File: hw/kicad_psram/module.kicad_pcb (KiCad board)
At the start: 8 copper layers, 110 x 70 mm, 20 parts

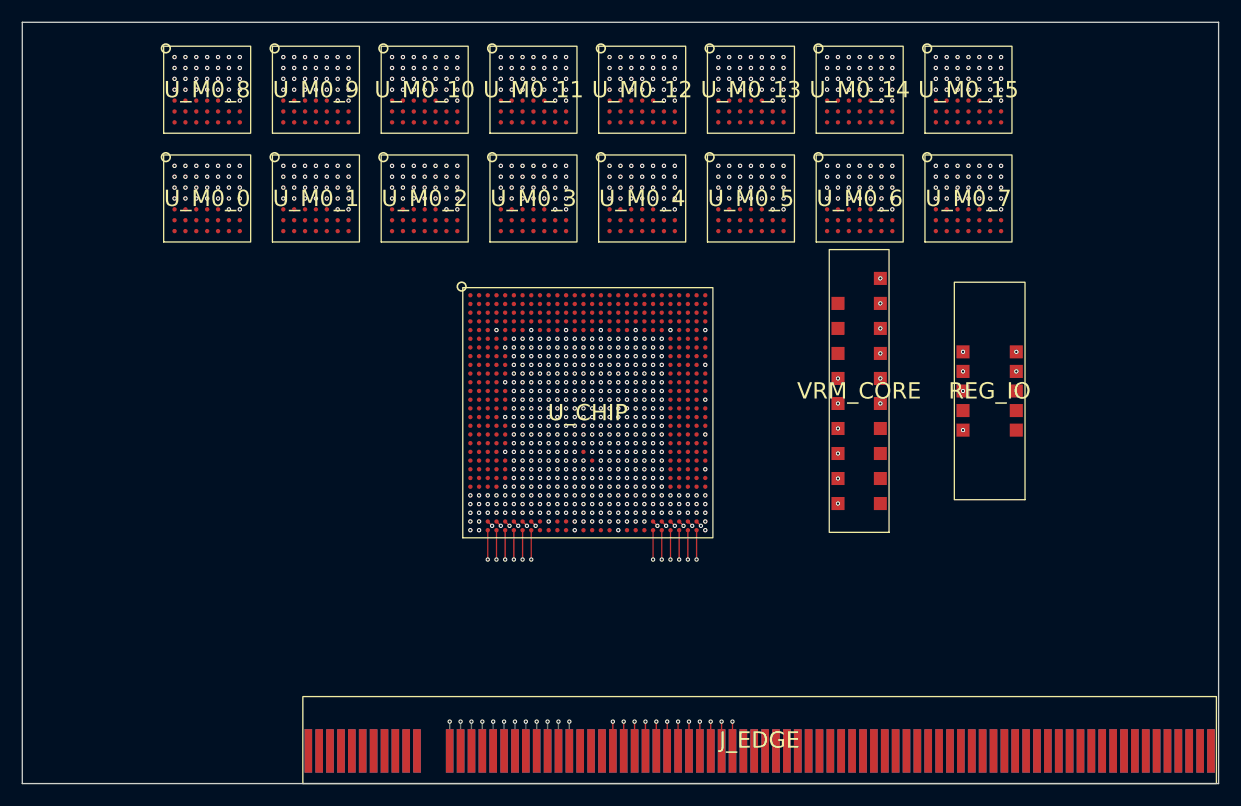
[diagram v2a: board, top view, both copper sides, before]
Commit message: Link in and out on the same finger positions: straight slot-to-slot hops
link_in sits on side A and link_out on side B of the same twelve edge
positions, so a slot's out-row pin faces the next slot's in-row pin and
every skip-one hop is a straight ribbon.  On the card the two drops from
the die's south-edge blocks lean towards one finger span from either side
and cross, so the out drop takes In3 and the two faces' vias interleave
half a position apart above the fingers.  The ribbon band narrows from
27 mm to 12, the stagger from 52 mm to 38, and the short board from 180 to
170 mm deep.  finger_layout: offset keeps the earlier separate spans.

Co-Authored-By: Claude Fable 5.1 <noreply@anthropic.com>
Claude-Session: https://claude.ai/code/session_01VmmvkZe8Ctg3RAykNGsQBn
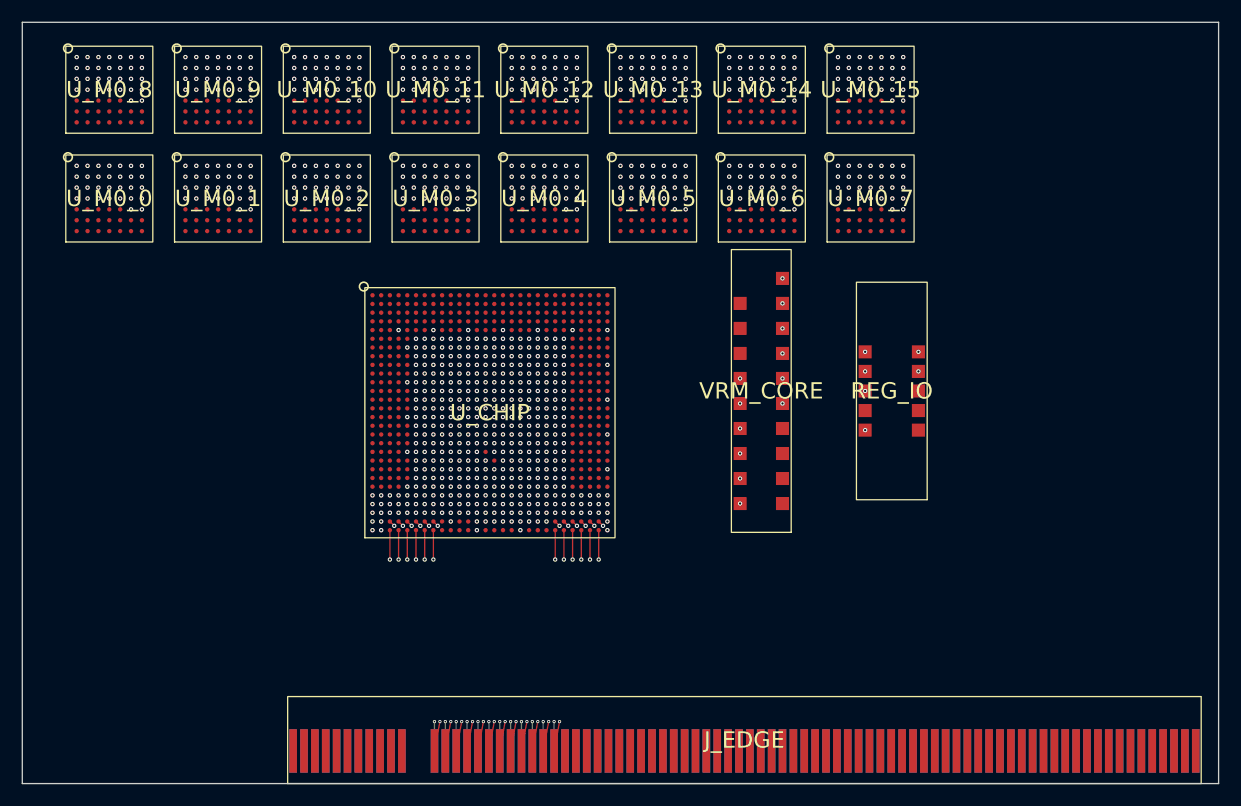
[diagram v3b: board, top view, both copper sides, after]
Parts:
- moved REG_IO 9.00 mm to (100.0, 53.9)
- moved U_CHIP 9.00 mm to (63.0, 55.9)
- moved U_M0_0 9.00 mm to (28.0, 36.2)
- moved U_M0_1 9.00 mm to (38.0, 36.2)
- moved U_M0_10 9.00 mm to (48.0, 26.2)
- moved U_M0_11 9.00 mm to (58.0, 26.2)
- moved U_M0_12 9.00 mm to (68.0, 26.2)
- moved U_M0_13 9.00 mm to (78.0, 26.2)
- moved U_M0_14 9.00 mm to (88.0, 26.2)
- moved U_M0_15 9.00 mm to (98.0, 26.2)
- moved U_M0_2 9.00 mm to (48.0, 36.2)
- moved U_M0_3 9.00 mm to (58.0, 36.2)
- moved U_M0_4 9.00 mm to (68.0, 36.2)
- moved U_M0_5 9.00 mm to (78.0, 36.2)
- moved U_M0_6 9.00 mm to (88.0, 36.2)
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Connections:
- J_EDGE pad B12: GND -> LINK_OUT_DATA0
- J_EDGE pad B13: GND -> LINK_OUT_DATA1
- J_EDGE pad B14: GND -> LINK_OUT_DATA2
- J_EDGE pad B15: GND -> LINK_OUT_DATA3
- J_EDGE pad B16: GND -> LINK_OUT_DATA4
- J_EDGE pad B17: GND -> LINK_OUT_DATA5
- J_EDGE pad B18: GND -> LINK_OUT_DATA6
- J_EDGE pad B19: GND -> LINK_OUT_DATA7
- J_EDGE pad B20: GND -> LINK_OUT_CLOCK
- J_EDGE pad B21: GND -> LINK_OUT_VALID
- J_EDGE pad B22: GND -> LINK_OUT_READY_BACK
- J_EDGE pad B23: GND -> LINK_OUT_SOF
- J_EDGE pad B27: LINK_OUT_DATA0 -> GND
- J_EDGE pad B28: LINK_OUT_DATA1 -> GND
- J_EDGE pad B29: LINK_OUT_DATA2 -> GND
- J_EDGE pad B30: LINK_OUT_DATA3 -> GND
- J_EDGE pad B31: LINK_OUT_DATA4 -> GND
- J_EDGE pad B32: LINK_OUT_DATA5 -> GND
- J_EDGE pad B33: LINK_OUT_DATA6 -> GND
- J_EDGE pad B34: LINK_OUT_DATA7 -> GND
- J_EDGE pad B35: LINK_OUT_CLOCK -> GND
- J_EDGE pad B36: LINK_OUT_VALID -> GND
- J_EDGE pad B37: LINK_OUT_READY_BACK -> GND
- J_EDGE pad B38: LINK_OUT_SOF -> GND
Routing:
- net LINK_IN_DATA0: track 21.3 -> 25.1 mm
- net LINK_OUT_SOF: track 22.3 -> 26.0 mm
- net LINK_IN_DATA1: track 21.9 -> 25.4 mm
- net LINK_OUT_READY_BACK: track 21.0 -> 24.4 mm
- net LINK_IN_DATA2: track 20.7 -> 23.9 mm
- net LINK_OUT_VALID: track 21.7 -> 24.8 mm
- net LINK_OUT_DATA0: track 21.3 -> 24.3 mm
- net LINK_IN_SOF: track 22.3 -> 25.3 mm
- net LINK_IN_READY_BACK: track 21.0 -> 23.9 mm
- net LINK_OUT_DATA1: track 22.0 -> 24.9 mm
- net LINK_IN_DATA3: track 21.5 -> 24.3 mm
- net LINK_IN_VALID: track 21.7 -> 24.5 mm
- net LINK_OUT_DATA2: track 20.7 -> 23.6 mm
- net LINK_OUT_CLOCK: track 20.5 -> 23.4 mm
- net LINK_IN_CLOCK: track 20.5 -> 23.2 mm
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
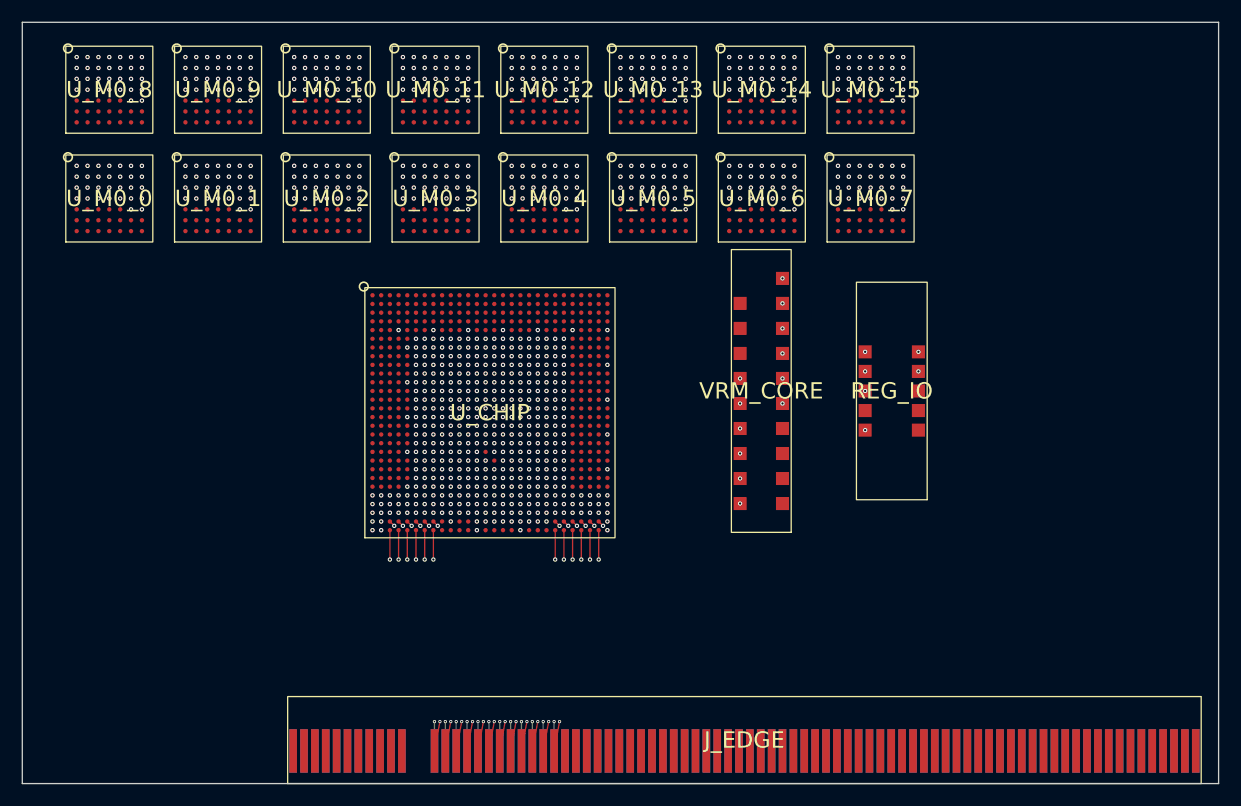
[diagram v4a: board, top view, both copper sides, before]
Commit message: Choose the PSRAM and write its HPI controller
The PSRAM board's device is the AP Memory APS512XXN-OB9-BG: 512 Mb, the
Xccela DDR interface in x16 (HPI) mode, 250 MHz, 1.8 V, a 24-ball 6 x 8
mm BGA.  fabric/hpi.py carries its geometry, the mode-register
encodings, the command frame and the striping of the die's memory port
over sixteen devices in page-sized stripes; fabric_hpi.sv is the
controller: a per-device channel with the power-up sequence, global
reset, mode registers and an identity check, the command phase on both
clock edges, fixed-latency writes with data mask, and reads captured by
the device's strobe through a gray-pointer ring so refresh push-out
costs nothing; and a stripe unit that splits a burst into concurrent
per-device chunks, returns read data in order and completes a write
only when every chunk is in the device.  A behavioural device model
checks the protocol (tCEM, tCPH, even addresses, x16 mode) and the
testbench runs random bursts over one, two, four and sixteen devices
against the striped image.

The memory port's burst count widens to 12 bits so a head's state is
one burst across all devices, and the map aligns regions to a page.
The board gains the real part, its DQS/DM naming, and the four shared
clocks as a small interface the pinout places with the management
signals and the card wires to its devices; the connector count is
unchanged.

Co-Authored-By: Claude Fable 5.1 <noreply@anthropic.com>
Claude-Session: https://claude.ai/code/session_01VmmvkZe8Ctg3RAykNGsQBn
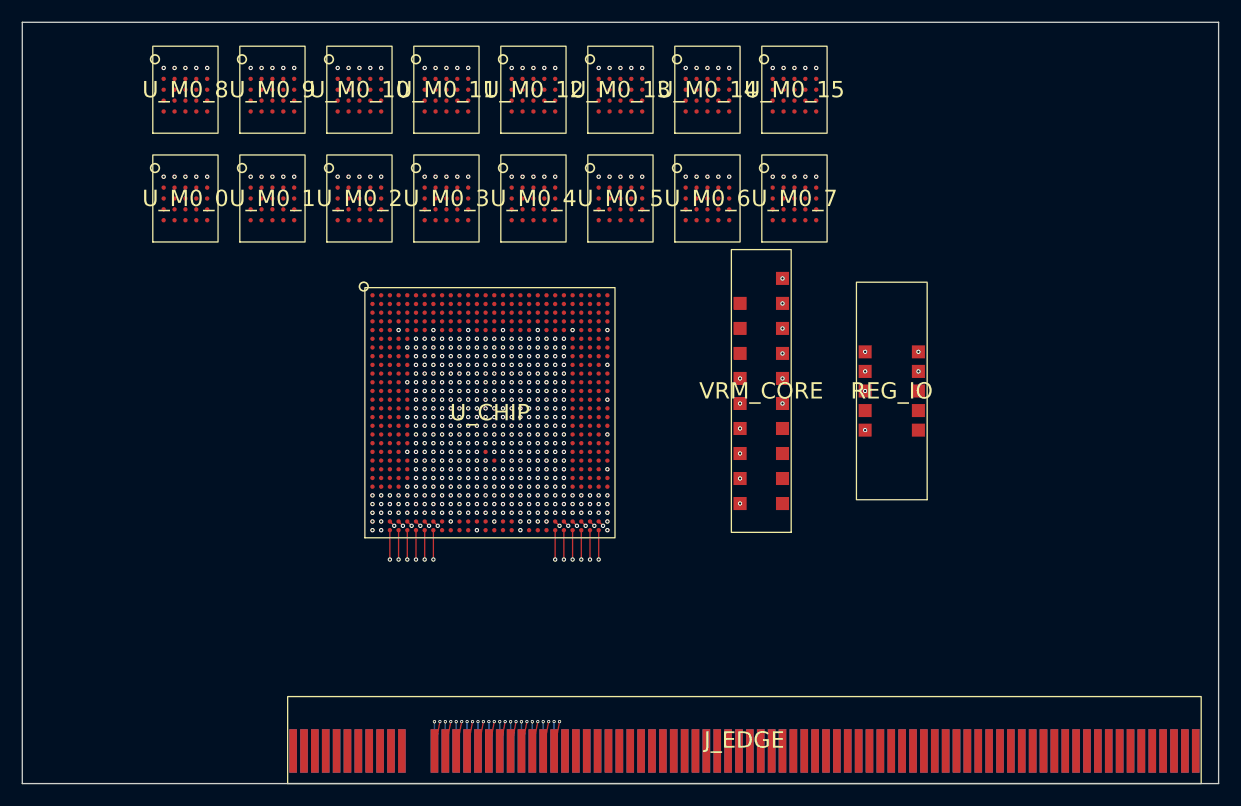
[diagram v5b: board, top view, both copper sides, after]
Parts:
- U_M0_0, U_M0_1, U_M0_10, U_M0_11, U_M0_12, U_M0_13, U_M0_14, U_M0_15, U_M0_2, U_M0_3, U_M0_4, U_M0_5, U_M0_6, U_M0_7, U_M0_8, U_M0_9: footprint appliance:FBGA49_7x7_P1.0 -> appliance:BGA24_5x5_P1.0
- moved U_M0_0 7.00 mm to (35.0, 36.2)
- moved U_M0_15 7.00 mm to (91.0, 26.2)
- moved U_M0_7 7.00 mm to (91.0, 36.2)
- moved U_M0_8 7.00 mm to (35.0, 26.2)
- moved U_M0_1 5.00 mm to (43.0, 36.2)
- moved U_M0_14 5.00 mm to (83.0, 26.2)
- moved U_M0_6 5.00 mm to (83.0, 36.2)
- moved U_M0_9 5.00 mm to (43.0, 26.2)
- moved U_M0_10 3.00 mm to (51.0, 26.2)
- moved U_M0_13 3.00 mm to (75.0, 26.2)
- moved U_M0_2 3.00 mm to (51.0, 36.2)
- moved U_M0_5 3.00 mm to (75.0, 36.2)
- moved U_M0_11 1.00 mm to (59.0, 26.2)
- moved U_M0_12 1.00 mm to (67.0, 26.2)
- moved U_M0_3 1.00 mm to (59.0, 36.2)
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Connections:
- net PSRAM_0_CS renamed PSRAM_0_CE
- net PSRAM_0_RWDS0 renamed PSRAM_0_DQS0
- net PSRAM_0_RWDS1 renamed PSRAM_0_DQS1
- net PSRAM_10_CS renamed PSRAM_10_CE
- net PSRAM_10_RWDS0 renamed PSRAM_10_DQS0
- net PSRAM_10_RWDS1 renamed PSRAM_10_DQS1
- net PSRAM_11_CS renamed PSRAM_11_CE
- net PSRAM_11_RWDS0 renamed PSRAM_11_DQS0
- net PSRAM_11_RWDS1 renamed PSRAM_11_DQS1
- net PSRAM_12_CS renamed PSRAM_12_CE
- net PSRAM_12_RWDS0 renamed PSRAM_12_DQS0
- net PSRAM_12_RWDS1 renamed PSRAM_12_DQS1
- net PSRAM_13_CS renamed PSRAM_13_CE
- net PSRAM_13_RWDS0 renamed PSRAM_13_DQS0
- net PSRAM_13_RWDS1 renamed PSRAM_13_DQS1
- net PSRAM_14_CS renamed PSRAM_14_CE
- net PSRAM_14_RWDS0 renamed PSRAM_14_DQS0
- net PSRAM_14_RWDS1 renamed PSRAM_14_DQS1
- net PSRAM_15_CS renamed PSRAM_15_CE
- net PSRAM_15_RWDS0 renamed PSRAM_15_DQS0
- net PSRAM_15_RWDS1 renamed PSRAM_15_DQS1
- net PSRAM_1_CS renamed PSRAM_1_CE
- net PSRAM_1_RWDS0 renamed PSRAM_1_DQS0
- net PSRAM_1_RWDS1 renamed PSRAM_1_DQS1
- net PSRAM_2_CS renamed PSRAM_2_CE
- net PSRAM_2_RWDS0 renamed PSRAM_2_DQS0
- net PSRAM_2_RWDS1 renamed PSRAM_2_DQS1
- net PSRAM_3_CS renamed PSRAM_3_CE
- net PSRAM_3_RWDS0 renamed PSRAM_3_DQS0
- net PSRAM_3_RWDS1 renamed PSRAM_3_DQS1
- net PSRAM_4_CS renamed PSRAM_4_CE
- net PSRAM_4_RWDS0 renamed PSRAM_4_DQS0
- net PSRAM_4_RWDS1 renamed PSRAM_4_DQS1
- net PSRAM_5_CS renamed PSRAM_5_CE
- net PSRAM_5_RWDS0 renamed PSRAM_5_DQS0
- net PSRAM_5_RWDS1 renamed PSRAM_5_DQS1
- net PSRAM_6_CS renamed PSRAM_6_CE
- net PSRAM_6_RWDS0 renamed PSRAM_6_DQS0
- net PSRAM_6_RWDS1 renamed PSRAM_6_DQS1
- net PSRAM_7_CS renamed PSRAM_7_CE
- net PSRAM_7_RWDS0 renamed PSRAM_7_DQS0
- net PSRAM_7_RWDS1 renamed PSRAM_7_DQS1
- net PSRAM_8_CS renamed PSRAM_8_CE
- net PSRAM_8_RWDS0 renamed PSRAM_8_DQS0
- net PSRAM_8_RWDS1 renamed PSRAM_8_DQS1
- net PSRAM_9_CS renamed PSRAM_9_CE
- net PSRAM_9_RWDS0 renamed PSRAM_9_DQS0
- net PSRAM_9_RWDS1 renamed PSRAM_9_DQS1
- U_CHIP pad AG13: GND -> PSRAM_CLK0
- U_CHIP pad AG14: VDD_CORE -> PSRAM_CLK1
- U_CHIP pad AG16: VDD_CORE -> PSRAM_CLK2
- U_CHIP pad AG17: GND -> PSRAM_CLK3
- U_M0_0 pad B1: VDD_IO_1V8 -> MEM0_DQ15
- U_M0_0 pad B2: GND -> MEM0_DQS0
- U_M0_0 pad B3: VDD_IO_1V8 -> MEM0_DQS1
- U_M0_0 pad B4: GND -> MEM0_CE
- U_M0_0 pad B5: VDD_IO_1V8 -> PSRAM_CLK0
- U_M0_0 pad C1: GND -> MEM0_DQ10
- U_M0_0 pad C2: VDD_IO_1V8 -> MEM0_DQ11
- U_M0_0 pad C3: GND -> MEM0_DQ12
- U_M0_0 pad C4: VDD_IO_1V8 -> MEM0_DQ13
- U_M0_0 pad C5: GND -> MEM0_DQ14
- U_M0_0 pad D1: VDD_IO_1V8 -> MEM0_DQ5
- U_M0_0 pad D2: GND -> MEM0_DQ6
- U_M0_0 pad D3: VDD_IO_1V8 -> MEM0_DQ7
- U_M0_0 pad D4: GND -> MEM0_DQ8
- U_M0_0 pad D5: VDD_IO_1V8 -> MEM0_DQ9
- U_M0_0 pad E1: MEM0_DQ14 -> MEM0_DQ0
- U_M0_0 pad E2: MEM0_DQ15 -> MEM0_DQ1
- U_M0_0 pad E3: MEM0_RWDS0 -> MEM0_DQ2
- U_M0_0 pad E4: MEM0_RWDS1 -> MEM0_DQ3
- U_M0_0 pad E5: MEM0_CS -> MEM0_DQ4
- U_M0_1 pad B1: VDD_IO_1V8 -> MEM1_DQ15
- U_M0_1 pad B2: GND -> MEM1_DQS0
- U_M0_1 pad B3: VDD_IO_1V8 -> MEM1_DQS1
- U_M0_1 pad B4: GND -> MEM1_CE
- U_M0_1 pad B5: VDD_IO_1V8 -> PSRAM_CLK0
- U_M0_1 pad C1: GND -> MEM1_DQ10
- U_M0_1 pad C2: VDD_IO_1V8 -> MEM1_DQ11
- U_M0_1 pad C3: GND -> MEM1_DQ12
- U_M0_1 pad C4: VDD_IO_1V8 -> MEM1_DQ13
- U_M0_1 pad C5: GND -> MEM1_DQ14
- U_M0_1 pad D1: VDD_IO_1V8 -> MEM1_DQ5
- U_M0_1 pad D2: GND -> MEM1_DQ6
- U_M0_1 pad D3: VDD_IO_1V8 -> MEM1_DQ7
- U_M0_1 pad D4: GND -> MEM1_DQ8
- U_M0_1 pad D5: VDD_IO_1V8 -> MEM1_DQ9
- U_M0_1 pad E1: MEM1_DQ14 -> MEM1_DQ0
- U_M0_1 pad E2: MEM1_DQ15 -> MEM1_DQ1
- U_M0_1 pad E3: MEM1_RWDS0 -> MEM1_DQ2
- U_M0_1 pad E4: MEM1_RWDS1 -> MEM1_DQ3
- U_M0_1 pad E5: MEM1_CS -> MEM1_DQ4
- U_M0_10 pad B1: VDD_IO_1V8 -> MEM10_DQ15
- U_M0_10 pad B2: GND -> MEM10_DQS0
- U_M0_10 pad B3: VDD_IO_1V8 -> MEM10_DQS1
- U_M0_10 pad B4: GND -> MEM10_CE
- U_M0_10 pad B5: VDD_IO_1V8 -> PSRAM_CLK2
- U_M0_10 pad C1: GND -> MEM10_DQ10
- U_M0_10 pad C2: VDD_IO_1V8 -> MEM10_DQ11
- U_M0_10 pad C3: GND -> MEM10_DQ12
- U_M0_10 pad C4: VDD_IO_1V8 -> MEM10_DQ13
- U_M0_10 pad C5: GND -> MEM10_DQ14
- U_M0_10 pad D1: VDD_IO_1V8 -> MEM10_DQ5
- U_M0_10 pad D2: GND -> MEM10_DQ6
- U_M0_10 pad D3: VDD_IO_1V8 -> MEM10_DQ7
- U_M0_10 pad D4: GND -> MEM10_DQ8
- U_M0_10 pad D5: VDD_IO_1V8 -> MEM10_DQ9
- U_M0_10 pad E1: MEM10_DQ14 -> MEM10_DQ0
- U_M0_10 pad E2: MEM10_DQ15 -> MEM10_DQ1
- U_M0_10 pad E3: MEM10_RWDS0 -> MEM10_DQ2
- U_M0_10 pad E4: MEM10_RWDS1 -> MEM10_DQ3
- U_M0_10 pad E5: MEM10_CS -> MEM10_DQ4
- U_M0_11 pad B1: VDD_IO_1V8 -> MEM11_DQ15
- U_M0_11 pad B2: GND -> MEM11_DQS0
- U_M0_11 pad B3: VDD_IO_1V8 -> MEM11_DQS1
- U_M0_11 pad B4: GND -> MEM11_CE
- U_M0_11 pad B5: VDD_IO_1V8 -> PSRAM_CLK2
- U_M0_11 pad C1: GND -> MEM11_DQ10
- U_M0_11 pad C2: VDD_IO_1V8 -> MEM11_DQ11
- U_M0_11 pad C3: GND -> MEM11_DQ12
- U_M0_11 pad C4: VDD_IO_1V8 -> MEM11_DQ13
- U_M0_11 pad C5: GND -> MEM11_DQ14
- U_M0_11 pad D1: VDD_IO_1V8 -> MEM11_DQ5
- U_M0_11 pad D2: GND -> MEM11_DQ6
- U_M0_11 pad D3: VDD_IO_1V8 -> MEM11_DQ7
- U_M0_11 pad D4: GND -> MEM11_DQ8
- U_M0_11 pad D5: VDD_IO_1V8 -> MEM11_DQ9
- U_M0_11 pad E1: MEM11_DQ14 -> MEM11_DQ0
- U_M0_11 pad E2: MEM11_DQ15 -> MEM11_DQ1
- U_M0_11 pad E3: MEM11_RWDS0 -> MEM11_DQ2
- U_M0_11 pad E4: MEM11_RWDS1 -> MEM11_DQ3
- U_M0_11 pad E5: MEM11_CS -> MEM11_DQ4
- U_M0_12 pad B1: VDD_IO_1V8 -> MEM12_DQ15
- U_M0_12 pad B2: GND -> MEM12_DQS0
- U_M0_12 pad B3: VDD_IO_1V8 -> MEM12_DQS1
- U_M0_12 pad B4: GND -> MEM12_CE
- U_M0_12 pad B5: VDD_IO_1V8 -> PSRAM_CLK3
- U_M0_12 pad C1: GND -> MEM12_DQ10
- U_M0_12 pad C2: VDD_IO_1V8 -> MEM12_DQ11
- U_M0_12 pad C3: GND -> MEM12_DQ12
- U_M0_12 pad C4: VDD_IO_1V8 -> MEM12_DQ13
- U_M0_12 pad C5: GND -> MEM12_DQ14
- U_M0_12 pad D1: VDD_IO_1V8 -> MEM12_DQ5
- U_M0_12 pad D2: GND -> MEM12_DQ6
- U_M0_12 pad D3: VDD_IO_1V8 -> MEM12_DQ7
- U_M0_12 pad D4: GND -> MEM12_DQ8
- U_M0_12 pad D5: VDD_IO_1V8 -> MEM12_DQ9
- U_M0_12 pad E1: MEM12_DQ14 -> MEM12_DQ0
- U_M0_12 pad E2: MEM12_DQ15 -> MEM12_DQ1
- U_M0_12 pad E3: MEM12_RWDS0 -> MEM12_DQ2
- U_M0_12 pad E4: MEM12_RWDS1 -> MEM12_DQ3
- U_M0_12 pad E5: MEM12_CS -> MEM12_DQ4
- U_M0_13 pad B1: VDD_IO_1V8 -> MEM13_DQ15
- U_M0_13 pad B2: GND -> MEM13_DQS0
- U_M0_13 pad B3: VDD_IO_1V8 -> MEM13_DQS1
- U_M0_13 pad B4: GND -> MEM13_CE
- U_M0_13 pad B5: VDD_IO_1V8 -> PSRAM_CLK3
- U_M0_13 pad C1: GND -> MEM13_DQ10
- U_M0_13 pad C2: VDD_IO_1V8 -> MEM13_DQ11
- U_M0_13 pad C3: GND -> MEM13_DQ12
- U_M0_13 pad C4: VDD_IO_1V8 -> MEM13_DQ13
- U_M0_13 pad C5: GND -> MEM13_DQ14
- U_M0_13 pad D1: VDD_IO_1V8 -> MEM13_DQ5
- U_M0_13 pad D2: GND -> MEM13_DQ6
- U_M0_13 pad D3: VDD_IO_1V8 -> MEM13_DQ7
- U_M0_13 pad D4: GND -> MEM13_DQ8
- U_M0_13 pad D5: VDD_IO_1V8 -> MEM13_DQ9
- U_M0_13 pad E1: MEM13_DQ14 -> MEM13_DQ0
- U_M0_13 pad E2: MEM13_DQ15 -> MEM13_DQ1
- U_M0_13 pad E3: MEM13_RWDS0 -> MEM13_DQ2
- U_M0_13 pad E4: MEM13_RWDS1 -> MEM13_DQ3
- U_M0_13 pad E5: MEM13_CS -> MEM13_DQ4
- U_M0_14 pad B1: VDD_IO_1V8 -> MEM14_DQ15
- U_M0_14 pad B2: GND -> MEM14_DQS0
- U_M0_14 pad B3: VDD_IO_1V8 -> MEM14_DQS1
- U_M0_14 pad B4: GND -> MEM14_CE
- U_M0_14 pad B5: VDD_IO_1V8 -> PSRAM_CLK3
- U_M0_14 pad C1: GND -> MEM14_DQ10
- U_M0_14 pad C2: VDD_IO_1V8 -> MEM14_DQ11
- U_M0_14 pad C3: GND -> MEM14_DQ12
- U_M0_14 pad C4: VDD_IO_1V8 -> MEM14_DQ13
- U_M0_14 pad C5: GND -> MEM14_DQ14
- U_M0_14 pad D1: VDD_IO_1V8 -> MEM14_DQ5
- U_M0_14 pad D2: GND -> MEM14_DQ6
- U_M0_14 pad D3: VDD_IO_1V8 -> MEM14_DQ7
- U_M0_14 pad D4: GND -> MEM14_DQ8
- U_M0_14 pad D5: VDD_IO_1V8 -> MEM14_DQ9
- U_M0_14 pad E1: MEM14_DQ14 -> MEM14_DQ0
- U_M0_14 pad E2: MEM14_DQ15 -> MEM14_DQ1
- U_M0_14 pad E3: MEM14_RWDS0 -> MEM14_DQ2
- U_M0_14 pad E4: MEM14_RWDS1 -> MEM14_DQ3
- U_M0_14 pad E5: MEM14_CS -> MEM14_DQ4
- U_M0_15 pad B1: VDD_IO_1V8 -> MEM15_DQ15
- U_M0_15 pad B2: GND -> MEM15_DQS0
- U_M0_15 pad B3: VDD_IO_1V8 -> MEM15_DQS1
- U_M0_15 pad B4: GND -> MEM15_CE
- U_M0_15 pad B5: VDD_IO_1V8 -> PSRAM_CLK3
- U_M0_15 pad C1: GND -> MEM15_DQ10
- U_M0_15 pad C2: VDD_IO_1V8 -> MEM15_DQ11
- U_M0_15 pad C3: GND -> MEM15_DQ12
- U_M0_15 pad C4: VDD_IO_1V8 -> MEM15_DQ13
- U_M0_15 pad C5: GND -> MEM15_DQ14
- U_M0_15 pad D1: VDD_IO_1V8 -> MEM15_DQ5
- U_M0_15 pad D2: GND -> MEM15_DQ6
- U_M0_15 pad D3: VDD_IO_1V8 -> MEM15_DQ7
- U_M0_15 pad D4: GND -> MEM15_DQ8
- U_M0_15 pad D5: VDD_IO_1V8 -> MEM15_DQ9
- U_M0_15 pad E1: MEM15_DQ14 -> MEM15_DQ0
- U_M0_15 pad E2: MEM15_DQ15 -> MEM15_DQ1
- U_M0_15 pad E3: MEM15_RWDS0 -> MEM15_DQ2
- U_M0_15 pad E4: MEM15_RWDS1 -> MEM15_DQ3
- U_M0_15 pad E5: MEM15_CS -> MEM15_DQ4
- U_M0_2 pad B1: VDD_IO_1V8 -> MEM2_DQ15
- U_M0_2 pad B2: GND -> MEM2_DQS0
- U_M0_2 pad B3: VDD_IO_1V8 -> MEM2_DQS1
- U_M0_2 pad B4: GND -> MEM2_CE
- U_M0_2 pad B5: VDD_IO_1V8 -> PSRAM_CLK0
- U_M0_2 pad C1: GND -> MEM2_DQ10
- U_M0_2 pad C2: VDD_IO_1V8 -> MEM2_DQ11
- U_M0_2 pad C3: GND -> MEM2_DQ12
- U_M0_2 pad C4: VDD_IO_1V8 -> MEM2_DQ13
- U_M0_2 pad C5: GND -> MEM2_DQ14
- U_M0_2 pad D1: VDD_IO_1V8 -> MEM2_DQ5
- U_M0_2 pad D2: GND -> MEM2_DQ6
- U_M0_2 pad D3: VDD_IO_1V8 -> MEM2_DQ7
- U_M0_2 pad D4: GND -> MEM2_DQ8
- U_M0_2 pad D5: VDD_IO_1V8 -> MEM2_DQ9
- U_M0_2 pad E1: MEM2_DQ14 -> MEM2_DQ0
- U_M0_2 pad E2: MEM2_DQ15 -> MEM2_DQ1
- U_M0_2 pad E3: MEM2_RWDS0 -> MEM2_DQ2
- U_M0_2 pad E4: MEM2_RWDS1 -> MEM2_DQ3
- U_M0_2 pad E5: MEM2_CS -> MEM2_DQ4
- U_M0_3 pad B1: VDD_IO_1V8 -> MEM3_DQ15
- U_M0_3 pad B2: GND -> MEM3_DQS0
- U_M0_3 pad B3: VDD_IO_1V8 -> MEM3_DQS1
- U_M0_3 pad B4: GND -> MEM3_CE
- U_M0_3 pad B5: VDD_IO_1V8 -> PSRAM_CLK0
- U_M0_3 pad C1: GND -> MEM3_DQ10
- U_M0_3 pad C2: VDD_IO_1V8 -> MEM3_DQ11
- U_M0_3 pad C3: GND -> MEM3_DQ12
- U_M0_3 pad C4: VDD_IO_1V8 -> MEM3_DQ13
- U_M0_3 pad C5: GND -> MEM3_DQ14
- U_M0_3 pad D1: VDD_IO_1V8 -> MEM3_DQ5
- U_M0_3 pad D2: GND -> MEM3_DQ6
- U_M0_3 pad D3: VDD_IO_1V8 -> MEM3_DQ7
- U_M0_3 pad D4: GND -> MEM3_DQ8
- U_M0_3 pad D5: VDD_IO_1V8 -> MEM3_DQ9
- U_M0_3 pad E1: MEM3_DQ14 -> MEM3_DQ0
- U_M0_3 pad E2: MEM3_DQ15 -> MEM3_DQ1
- U_M0_3 pad E3: MEM3_RWDS0 -> MEM3_DQ2
- U_M0_3 pad E4: MEM3_RWDS1 -> MEM3_DQ3
- U_M0_3 pad E5: MEM3_CS -> MEM3_DQ4
- U_M0_4 pad B1: VDD_IO_1V8 -> MEM4_DQ15
- U_M0_4 pad B2: GND -> MEM4_DQS0
- U_M0_4 pad B3: VDD_IO_1V8 -> MEM4_DQS1
- U_M0_4 pad B4: GND -> MEM4_CE
- U_M0_4 pad B5: VDD_IO_1V8 -> PSRAM_CLK1
- U_M0_4 pad C1: GND -> MEM4_DQ10
- U_M0_4 pad C2: VDD_IO_1V8 -> MEM4_DQ11
- U_M0_4 pad C3: GND -> MEM4_DQ12
- U_M0_4 pad C4: VDD_IO_1V8 -> MEM4_DQ13
- U_M0_4 pad C5: GND -> MEM4_DQ14
- U_M0_4 pad D1: VDD_IO_1V8 -> MEM4_DQ5
- U_M0_4 pad D2: GND -> MEM4_DQ6
- U_M0_4 pad D3: VDD_IO_1V8 -> MEM4_DQ7
- U_M0_4 pad D4: GND -> MEM4_DQ8
- U_M0_4 pad D5: VDD_IO_1V8 -> MEM4_DQ9
- U_M0_4 pad E1: MEM4_DQ14 -> MEM4_DQ0
- U_M0_4 pad E2: MEM4_DQ15 -> MEM4_DQ1
- U_M0_4 pad E3: MEM4_RWDS0 -> MEM4_DQ2
- U_M0_4 pad E4: MEM4_RWDS1 -> MEM4_DQ3
- U_M0_4 pad E5: MEM4_CS -> MEM4_DQ4
- U_M0_5 pad B1: VDD_IO_1V8 -> MEM5_DQ15
- U_M0_5 pad B2: GND -> MEM5_DQS0
- U_M0_5 pad B3: VDD_IO_1V8 -> MEM5_DQS1
- U_M0_5 pad B4: GND -> MEM5_CE
- U_M0_5 pad B5: VDD_IO_1V8 -> PSRAM_CLK1
- U_M0_5 pad C1: GND -> MEM5_DQ10
- U_M0_5 pad C2: VDD_IO_1V8 -> MEM5_DQ11
- U_M0_5 pad C3: GND -> MEM5_DQ12
- U_M0_5 pad C4: VDD_IO_1V8 -> MEM5_DQ13
- U_M0_5 pad C5: GND -> MEM5_DQ14
- U_M0_5 pad D1: VDD_IO_1V8 -> MEM5_DQ5
- U_M0_5 pad D2: GND -> MEM5_DQ6
- U_M0_5 pad D3: VDD_IO_1V8 -> MEM5_DQ7
- U_M0_5 pad D4: GND -> MEM5_DQ8
- U_M0_5 pad D5: VDD_IO_1V8 -> MEM5_DQ9
- U_M0_5 pad E1: MEM5_DQ14 -> MEM5_DQ0
- U_M0_5 pad E2: MEM5_DQ15 -> MEM5_DQ1
- U_M0_5 pad E3: MEM5_RWDS0 -> MEM5_DQ2
- U_M0_5 pad E4: MEM5_RWDS1 -> MEM5_DQ3
- U_M0_5 pad E5: MEM5_CS -> MEM5_DQ4
- U_M0_6 pad B1: VDD_IO_1V8 -> MEM6_DQ15
- U_M0_6 pad B2: GND -> MEM6_DQS0
- U_M0_6 pad B3: VDD_IO_1V8 -> MEM6_DQS1
- U_M0_6 pad B4: GND -> MEM6_CE
- U_M0_6 pad B5: VDD_IO_1V8 -> PSRAM_CLK1
- U_M0_6 pad C1: GND -> MEM6_DQ10
- U_M0_6 pad C2: VDD_IO_1V8 -> MEM6_DQ11
- U_M0_6 pad C3: GND -> MEM6_DQ12
- U_M0_6 pad C4: VDD_IO_1V8 -> MEM6_DQ13
- U_M0_6 pad C5: GND -> MEM6_DQ14
- U_M0_6 pad D1: VDD_IO_1V8 -> MEM6_DQ5
- U_M0_6 pad D2: GND -> MEM6_DQ6
- U_M0_6 pad D3: VDD_IO_1V8 -> MEM6_DQ7
- U_M0_6 pad D4: GND -> MEM6_DQ8
- U_M0_6 pad D5: VDD_IO_1V8 -> MEM6_DQ9
- U_M0_6 pad E1: MEM6_DQ14 -> MEM6_DQ0
- U_M0_6 pad E2: MEM6_DQ15 -> MEM6_DQ1
- U_M0_6 pad E3: MEM6_RWDS0 -> MEM6_DQ2
- U_M0_6 pad E4: MEM6_RWDS1 -> MEM6_DQ3
- U_M0_6 pad E5: MEM6_CS -> MEM6_DQ4
- U_M0_7 pad B1: VDD_IO_1V8 -> MEM7_DQ15
- U_M0_7 pad B2: GND -> MEM7_DQS0
- U_M0_7 pad B3: VDD_IO_1V8 -> MEM7_DQS1
- U_M0_7 pad B4: GND -> MEM7_CE
- U_M0_7 pad B5: VDD_IO_1V8 -> PSRAM_CLK1
- U_M0_7 pad C1: GND -> MEM7_DQ10
- U_M0_7 pad C2: VDD_IO_1V8 -> MEM7_DQ11
- U_M0_7 pad C3: GND -> MEM7_DQ12
- U_M0_7 pad C4: VDD_IO_1V8 -> MEM7_DQ13
- U_M0_7 pad C5: GND -> MEM7_DQ14
- U_M0_7 pad D1: VDD_IO_1V8 -> MEM7_DQ5
- U_M0_7 pad D2: GND -> MEM7_DQ6
- U_M0_7 pad D3: VDD_IO_1V8 -> MEM7_DQ7
- U_M0_7 pad D4: GND -> MEM7_DQ8
- U_M0_7 pad D5: VDD_IO_1V8 -> MEM7_DQ9
- U_M0_7 pad E1: MEM7_DQ14 -> MEM7_DQ0
- U_M0_7 pad E2: MEM7_DQ15 -> MEM7_DQ1
- U_M0_7 pad E3: MEM7_RWDS0 -> MEM7_DQ2
- U_M0_7 pad E4: MEM7_RWDS1 -> MEM7_DQ3
- U_M0_7 pad E5: MEM7_CS -> MEM7_DQ4
- U_M0_8 pad B1: VDD_IO_1V8 -> MEM8_DQ15
- U_M0_8 pad B2: GND -> MEM8_DQS0
- U_M0_8 pad B3: VDD_IO_1V8 -> MEM8_DQS1
- U_M0_8 pad B4: GND -> MEM8_CE
- U_M0_8 pad B5: VDD_IO_1V8 -> PSRAM_CLK2
- U_M0_8 pad C1: GND -> MEM8_DQ10
- U_M0_8 pad C2: VDD_IO_1V8 -> MEM8_DQ11
- U_M0_8 pad C3: GND -> MEM8_DQ12
- U_M0_8 pad C4: VDD_IO_1V8 -> MEM8_DQ13
- U_M0_8 pad C5: GND -> MEM8_DQ14
- U_M0_8 pad D1: VDD_IO_1V8 -> MEM8_DQ5
- U_M0_8 pad D2: GND -> MEM8_DQ6
- U_M0_8 pad D3: VDD_IO_1V8 -> MEM8_DQ7
- U_M0_8 pad D4: GND -> MEM8_DQ8
- U_M0_8 pad D5: VDD_IO_1V8 -> MEM8_DQ9
- U_M0_8 pad E1: MEM8_DQ14 -> MEM8_DQ0
- U_M0_8 pad E2: MEM8_DQ15 -> MEM8_DQ1
- U_M0_8 pad E3: MEM8_RWDS0 -> MEM8_DQ2
- U_M0_8 pad E4: MEM8_RWDS1 -> MEM8_DQ3
- U_M0_8 pad E5: MEM8_CS -> MEM8_DQ4
- U_M0_9 pad B1: VDD_IO_1V8 -> MEM9_DQ15
- U_M0_9 pad B2: GND -> MEM9_DQS0
- U_M0_9 pad B3: VDD_IO_1V8 -> MEM9_DQS1
- U_M0_9 pad B4: GND -> MEM9_CE
- U_M0_9 pad B5: VDD_IO_1V8 -> PSRAM_CLK2
- U_M0_9 pad C1: GND -> MEM9_DQ10
- U_M0_9 pad C2: VDD_IO_1V8 -> MEM9_DQ11
- U_M0_9 pad C3: GND -> MEM9_DQ12
- U_M0_9 pad C4: VDD_IO_1V8 -> MEM9_DQ13
- U_M0_9 pad C5: GND -> MEM9_DQ14
- U_M0_9 pad D1: VDD_IO_1V8 -> MEM9_DQ5
- U_M0_9 pad D2: GND -> MEM9_DQ6
- U_M0_9 pad D3: VDD_IO_1V8 -> MEM9_DQ7
- U_M0_9 pad D4: GND -> MEM9_DQ8
- U_M0_9 pad D5: VDD_IO_1V8 -> MEM9_DQ9
- U_M0_9 pad E1: MEM9_DQ14 -> MEM9_DQ0
- U_M0_9 pad E2: MEM9_DQ15 -> MEM9_DQ1
- U_M0_9 pad E3: MEM9_RWDS0 -> MEM9_DQ2
- U_M0_9 pad E4: MEM9_RWDS1 -> MEM9_DQ3
- U_M0_9 pad E5: MEM9_CS -> MEM9_DQ4
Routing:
- net VDD_IO_1V8: vias 267 -> 59
- net VDD_CORE: vias 191 -> 189
- net GND: vias 480 -> 286

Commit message: Add the PHY delay lines with their DLL, and settle the PSRAM clock by simulation
fabric_phy.sv is the PHY: a behavioural 256-tap delay line and a master
DLL that measures the clock period in taps with a replica line and a
phase detector, walking the code through one period and then dithering
a tap either side of it; the quarter code drives the slave lines (the
device clock and the two DQS strobes per channel), which take a new
code only while every channel has CE# high.  A line that cannot span
the period is reported rather than searched forever.  The channel
waits for the lock before starting the device, and tb_hpi and
tb_mem_bridge run the whole controller through the delay lines at taps
of 25 to 90 ps in place of the ideal quarter-period delays.

hw/si.py is a small time-domain solver for lossless transmission-line
networks (LC ladder, 1 mm segments, 2 ps steps, Thevenin driver, the
datasheet's 5 pF package input per receiver) and hw/si_psram_clock.md
its answer to whether four devices can share one 250 MHz clock: the
star of four and the fly-by, terminated or not, cannot meet the
device's 0.6 ns edge without ringing past its absolute maximum, two per
clock passes only in a narrow band, and one clock per device passes
from 33 to 50 ohm at every length on the card.  The board takes a
clock per device: sixteen psram_clk balls, the small interfaces
allowed a third row on the south edge, the card's nets one per device,
the derived pinout and KiCad outputs regenerated.

Co-Authored-By: Claude Fable 5.1 <noreply@anthropic.com>
Claude-Session: https://claude.ai/code/session_01VmmvkZe8Ctg3RAykNGsQBn
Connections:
- U_CHIP pad AF10: GND -> PSRAM_CLK13
- U_CHIP pad AF11: VDD_CORE -> GND
- U_CHIP pad AF12: GND -> PSRAM_CLK14
- U_CHIP pad AF13: VDD_CORE -> PSRAM_CLK15
- U_CHIP pad AF3: VDD_CORE -> PSRAM_CLK7
- U_CHIP pad AF4: GND -> PSRAM_CLK8
- U_CHIP pad AF5: VDD_CORE -> PSRAM_CLK9
- U_CHIP pad AF7: VDD_CORE -> PSRAM_CLK10
- U_CHIP pad AF8: GND -> PSRAM_CLK11
- U_CHIP pad AF9: VDD_CORE -> PSRAM_CLK12
- U_CHIP pad AG18: VDD_CORE -> PSRAM_CLK4
- U_CHIP pad AG19: GND -> PSRAM_CLK5
- U_CHIP pad AG20: VDD_CORE -> GND
- U_CHIP pad AG21: GND -> PSRAM_CLK6
- U_M0_1 pad B5: PSRAM_CLK0 -> PSRAM_CLK1
- U_M0_10 pad B5: PSRAM_CLK2 -> PSRAM_CLK10
- U_M0_11 pad B5: PSRAM_CLK2 -> PSRAM_CLK11
- U_M0_12 pad B5: PSRAM_CLK3 -> PSRAM_CLK12
- U_M0_13 pad B5: PSRAM_CLK3 -> PSRAM_CLK13
- U_M0_14 pad B5: PSRAM_CLK3 -> PSRAM_CLK14
- U_M0_15 pad B5: PSRAM_CLK3 -> PSRAM_CLK15
- U_M0_2 pad B5: PSRAM_CLK0 -> PSRAM_CLK2
- U_M0_3 pad B5: PSRAM_CLK0 -> PSRAM_CLK3
- U_M0_4 pad B5: PSRAM_CLK1 -> PSRAM_CLK4
- U_M0_5 pad B5: PSRAM_CLK1 -> PSRAM_CLK5
- U_M0_6 pad B5: PSRAM_CLK1 -> PSRAM_CLK6
- U_M0_7 pad B5: PSRAM_CLK1 -> PSRAM_CLK7
- U_M0_8 pad B5: PSRAM_CLK2 -> PSRAM_CLK8
- U_M0_9 pad B5: PSRAM_CLK2 -> PSRAM_CLK9
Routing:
- net VDD_CORE: vias 189 -> 181
- net GND: vias 286 -> 282
